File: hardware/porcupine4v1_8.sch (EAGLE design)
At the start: 32 parts, among them X1 PROGCON

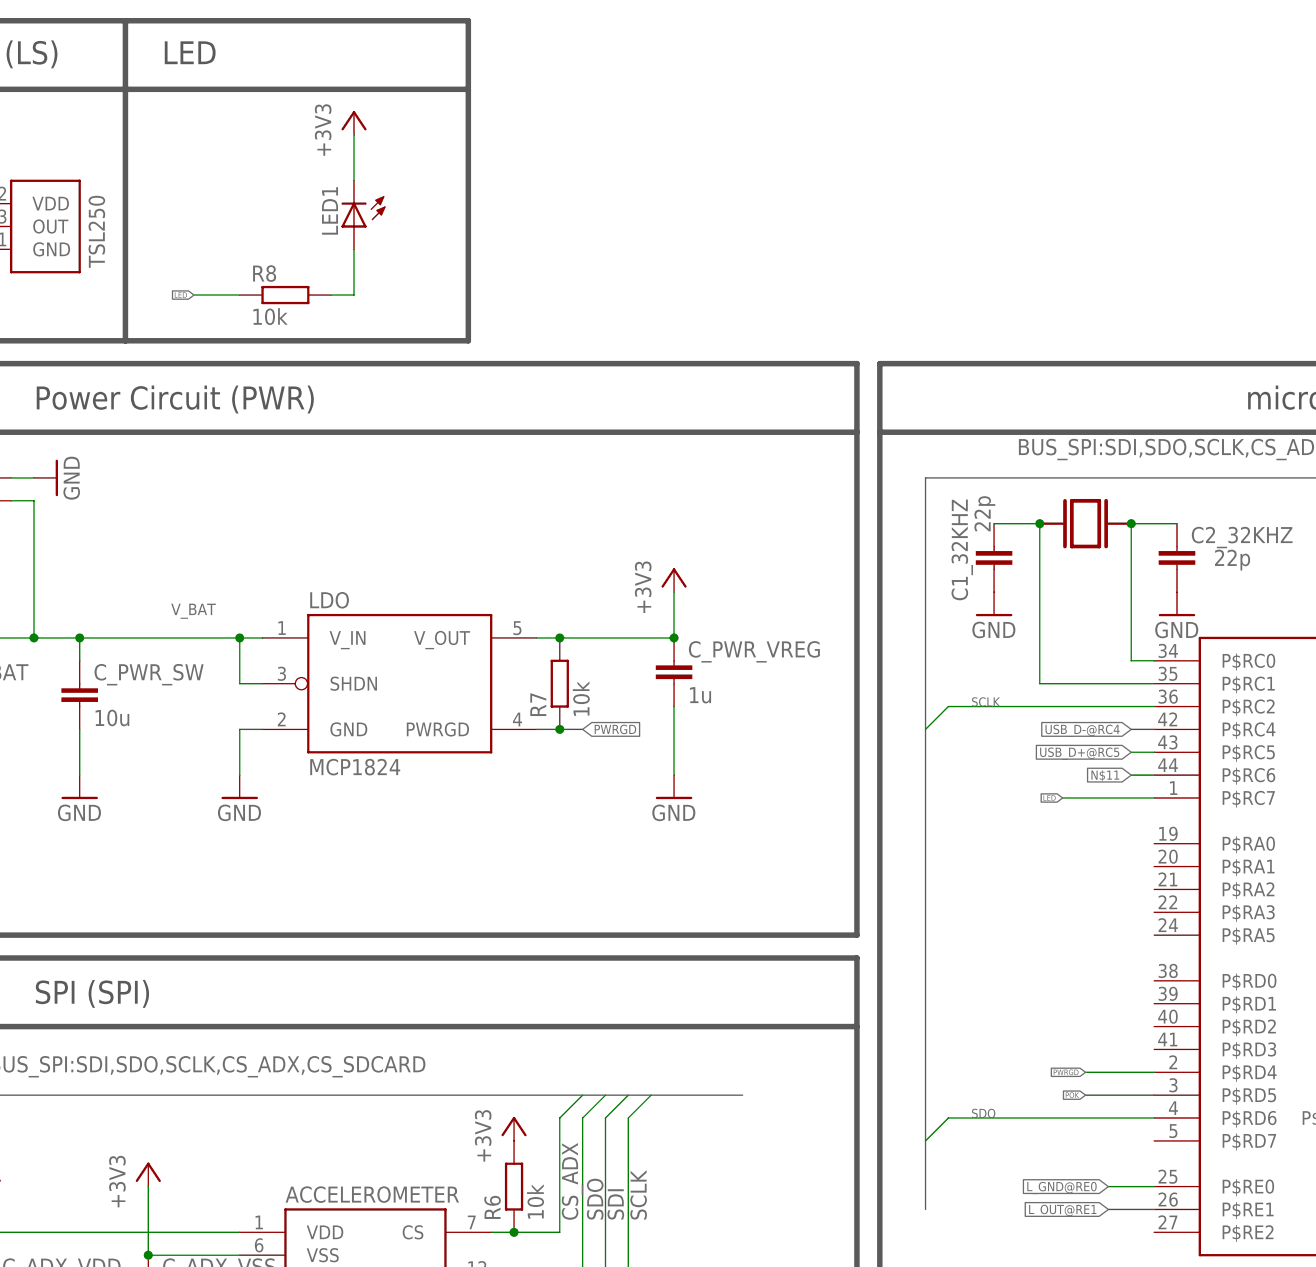
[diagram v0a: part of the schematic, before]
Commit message: porcupine4v1_8: added extension pins
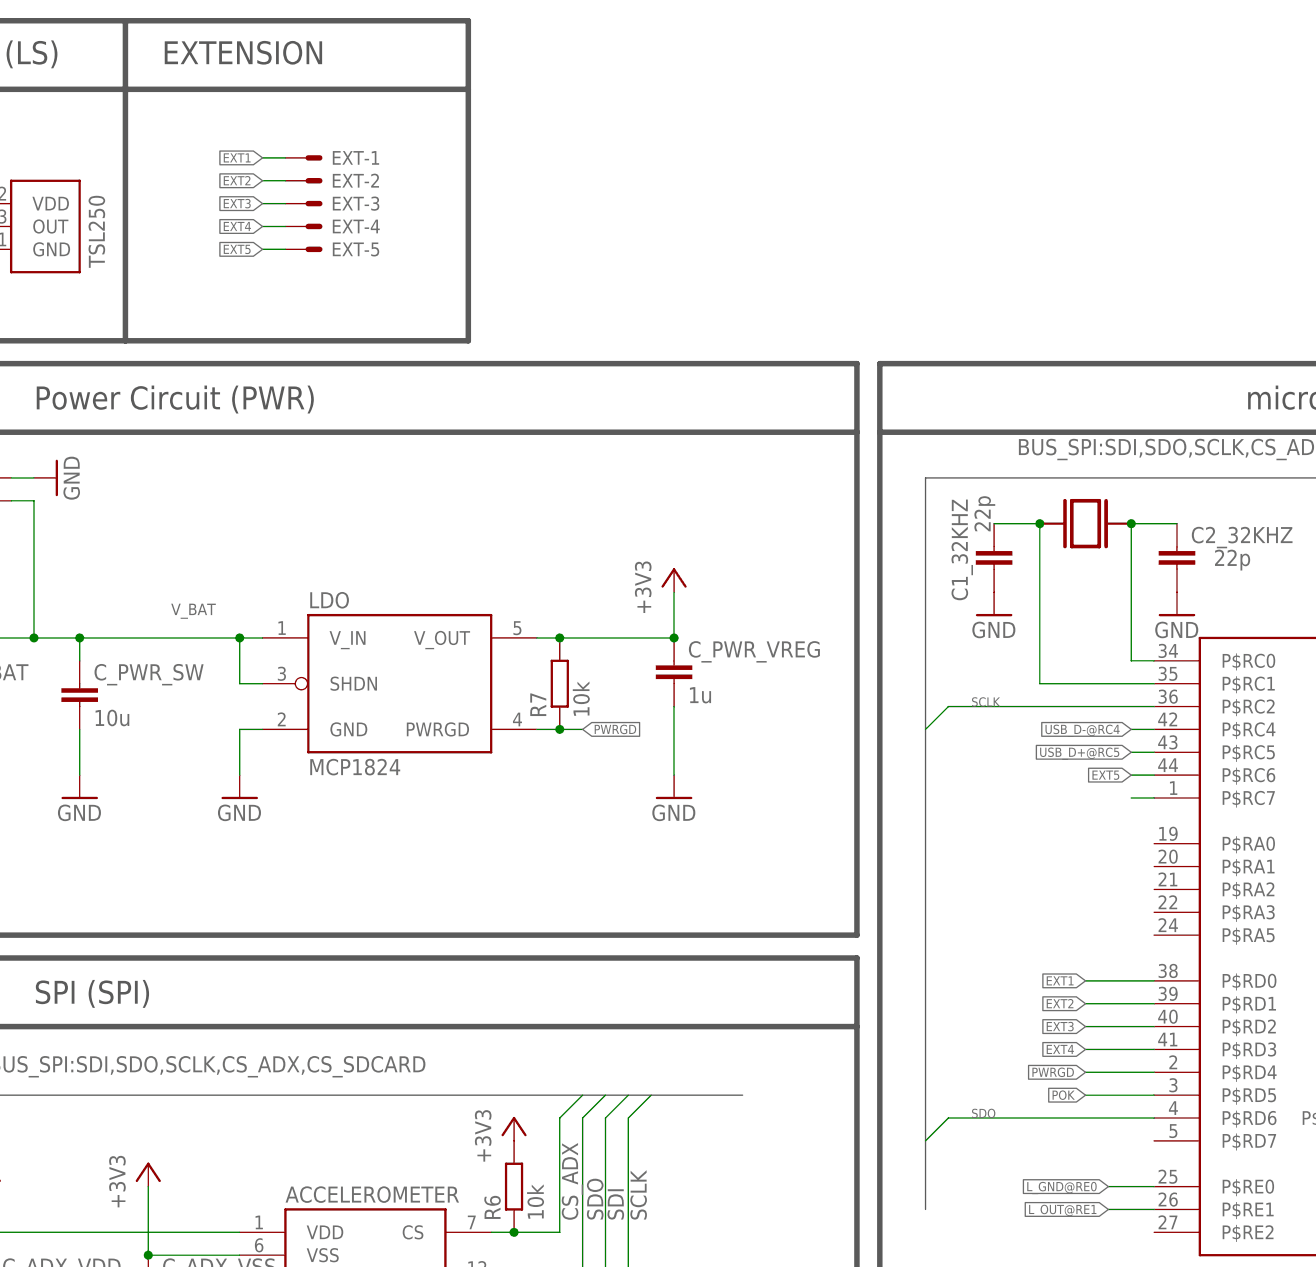
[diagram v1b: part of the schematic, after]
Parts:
- removed LED1: (no value), led:LEDCHIPLED_0805
- removed R8: 10k, rcl:R-EU_R0603
- added EXT: PROGCON, HedgehogLib:PROGCON
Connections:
- removed net LED: PIC_CONTROLLER.P$RC7, R8.1
- removed net N$11: PIC_CONTROLLER.P$RC6
- new net EXT1: EXT-1.S, PIC_CONTROLLER.P$RD0
- new net EXT2: EXT-2.S, PIC_CONTROLLER.P$RD1
- new net EXT3: EXT-3.S, PIC_CONTROLLER.P$RD2
- new net EXT4: EXT-4.S, PIC_CONTROLLER.P$RD3
- new net EXT5: EXT-5.S, PIC_CONTROLLER.P$RC6
- net +3V3: no longer LED1.C
- net N$4: now also PIC_CONTROLLER.P$RC7; no longer LED1.A, R8.2
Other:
- note added: "EXTENSION"
- note removed: "LED"
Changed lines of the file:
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@@
 <part name="LDO" library="HedgehogLib" deviceset="MCP1824" device=""/>
 <part name="BAT" library="con-molex" deviceset="53?-02" device="048"/>
-<part name="R8" library="rcl" deviceset="R-EU_" device="R0603" value="10k"/>
-<part name="+3V12" library="supply1" deviceset="+3V3" device=""/>
-<part name="LED1" library="led" deviceset="LED" device="CHIPLED_0805"/>
+<part name="EXT" library="HedgehogLib" deviceset="PROGCON" device=""/>
 </parts>
 <sheets>
@@
 <wire x1="132.08" y1="132.08" x2="132.08" y2="160.02" width="0.6096" layer="97"/>
 <wire x1="93.98" y1="132.08" x2="132.08" y2="132.08" width="0.6096" layer="97"/>
-<text x="98.044" y="162.814" size="2.54" layer="97">LED</text>
+<text x="98.044" y="162.814" size="2.54" layer="97">EXTENSION</text>
 </plain>
 <instances>
@@
 <instance part="BAT" gate="-1" x="78.74" y="114.3" rot="R180"/>
 <instance part="BAT" gate="-2" x="78.74" y="116.84" rot="R180"/>
-<instance part="R8" gate="G$1" x="111.76" y="137.16"/>
-<instance part="+3V12" gate="G$1" x="119.38" y="157.48"/>
-<instance part="LED1" gate="G$1" x="119.38" y="144.78" rot="R180"/>
+<instance part="EXT" gate="-1" x="114.3" y="152.4" smashed="yes">
+<attribute name="NAME" x="116.84" y="151.638" size="1.524" layer="95"/>
+</instance>
+<instance part="EXT" gate="-2" x="114.3" y="149.86"/>
+<instance part="EXT" gate="-3" x="114.3" y="147.32"/>
+<instance part="EXT" gate="-4" x="114.3" y="144.78"/>
+<instance part="EXT" gate="-5" x="114.3" y="142.24"/>
 </instances>
 <busses>
@@
 <pinref part="+3V17" gate="G$1" pin="+3V3"/>
 <pinref part="R3" gate="G$1" pin="2"/>
-</segment>
-<segment>
-<pinref part="+3V12" gate="G$1" pin="+3V3"/>
-<pinref part="LED1" gate="G$1" pin="C"/>
-<wire x1="119.38" y1="149.86" x2="119.38" y2="154.94" width="0.1524" layer="91"/>
 </segment>
 </net>
@@
 <pinref part="PIC_CONTROLLER" gate="G$1" pin="P$RD5"/>
 <wire x1="208.28" y1="48.26" x2="200.66" y2="48.26" width="0.1524" layer="91"/>
-<label x="200.66" y="48.26" size="0.6096" layer="95" rot="R180" xref="yes"/>
+<label x="200.66" y="48.26" size="1.016" layer="95" rot="R180" xref="yes"/>
 </segment>
 </net>
@@
 <pinref part="12MHZ_RESONATOR" gate="G$1" pin="1"/>
 <wire x1="243.84" y1="55.88" x2="259.08" y2="55.88" width="0.1524" layer="91"/>
-</segment>
-</net>
-<net name="N$11" class="0">
-<segment>
-<pinref part="PIC_CONTROLLER" gate="G$1" pin="P$RC6"/>
-<wire x1="208.28" y1="83.82" x2="205.74" y2="83.82" width="0.1524" layer="91"/>
-<label x="205.74" y="83.82" size="1.016" layer="95" rot="R180" xref="yes"/>
 </segment>
 </net>
@@
 <pinref part="PIC_CONTROLLER" gate="G$1" pin="P$RD4"/>
 <wire x1="208.28" y1="50.8" x2="200.66" y2="50.8" width="0.1524" layer="91"/>
-<label x="200.66" y="50.8" size="0.6096" layer="95" rot="R180" xref="yes"/>
-</segment>
-</net>
-<net name="LED" class="0">
+<label x="200.66" y="50.8" size="1.016" layer="95" rot="R180" xref="yes"/>
+</segment>
+</net>
+<net name="EXT1" class="0">
+<segment>
+<pinref part="EXT" gate="-1" pin="S"/>
+<wire x1="111.76" y1="152.4" x2="109.22" y2="152.4" width="0.1524" layer="91"/>
+<label x="109.22" y="152.4" size="1.016" layer="95" rot="R180" xref="yes"/>
+</segment>
+<segment>
+<pinref part="PIC_CONTROLLER" gate="G$1" pin="P$RD0"/>
+<wire x1="208.28" y1="60.96" x2="200.66" y2="60.96" width="0.1524" layer="91"/>
+<label x="200.66" y="60.96" size="1.016" layer="95" rot="R180" xref="yes"/>
+</segment>
+</net>
+<net name="EXT2" class="0">
+<segment>
+<pinref part="EXT" gate="-2" pin="S"/>
+<wire x1="111.76" y1="149.86" x2="109.22" y2="149.86" width="0.1524" layer="91"/>
+<label x="109.22" y="149.86" size="1.016" layer="95" rot="R180" xref="yes"/>
+</segment>
+<segment>
+<pinref part="PIC_CONTROLLER" gate="G$1" pin="P$RD1"/>
+<wire x1="208.28" y1="58.42" x2="200.66" y2="58.42" width="0.1524" layer="91"/>
+<label x="200.66" y="58.42" size="1.016" layer="95" rot="R180" xref="yes"/>
+</segment>
+</net>
+<net name="EXT3" class="0">
+<segment>
+<pinref part="EXT" gate="-3" pin="S"/>
+<wire x1="111.76" y1="147.32" x2="109.22" y2="147.32" width="0.1524" layer="91"/>
+<label x="109.22" y="147.32" size="1.016" layer="95" rot="R180" xref="yes"/>
+</segment>
+<segment>
+<pinref part="PIC_CONTROLLER" gate="G$1" pin="P$RD2"/>
+<wire x1="208.28" y1="55.88" x2="200.66" y2="55.88" width="0.1524" layer="91"/>
+<label x="200.66" y="55.88" size="1.016" layer="95" rot="R180" xref="yes"/>
+</segment>
+</net>
+<net name="EXT4" class="0">
+<segment>
+<pinref part="EXT" gate="-4" pin="S"/>
+<wire x1="111.76" y1="144.78" x2="109.22" y2="144.78" width="0.1524" layer="91"/>
+<label x="109.22" y="144.78" size="1.016" layer="95" rot="R180" xref="yes"/>
+</segment>
+<segment>
+<pinref part="PIC_CONTROLLER" gate="G$1" pin="P$RD3"/>
+<wire x1="208.28" y1="53.34" x2="200.66" y2="53.34" width="0.1524" layer="91"/>
+<label x="200.66" y="53.34" size="1.016" layer="95" rot="R180" xref="yes"/>
+</segment>
+</net>
+<net name="EXT5" class="0">
+<segment>
+<pinref part="EXT" gate="-5" pin="S"/>
+<wire x1="111.76" y1="142.24" x2="109.22" y2="142.24" width="0.1524" layer="91"/>
+<label x="109.22" y="142.24" size="1.016" layer="95" rot="R180" xref="yes"/>
+</segment>
+<segment>
+<pinref part="PIC_CONTROLLER" gate="G$1" pin="P$RC6"/>
+<wire x1="208.28" y1="83.82" x2="205.74" y2="83.82" width="0.1524" layer="91"/>
+<label x="205.74" y="83.82" size="1.016" layer="95" rot="R180" xref="yes"/>
+</segment>
+</net>
+<net name="N$4" class="0">
 <segment>
 <pinref part="PIC_CONTROLLER" gate="G$1" pin="P$RC7"/>
-<wire x1="208.28" y1="81.28" x2="198.12" y2="81.28" width="0.1524" layer="91"/>
-<label x="198.12" y="81.28" size="0.6096" layer="95" rot="R180" xref="yes"/>
-</segment>
-<segment>
-<pinref part="R8" gate="G$1" pin="1"/>
-<wire x1="106.68" y1="137.16" x2="101.6" y2="137.16" width="0.1524" layer="91"/>
-<label x="101.6" y="137.16" size="0.6096" layer="95" rot="R180" xref="yes"/>
-</segment>
-</net>
-<net name="N$4" class="0">
-<segment>
-<pinref part="R8" gate="G$1" pin="2"/>
-<pinref part="LED1" gate="G$1" pin="A"/>
-<wire x1="119.38" y1="142.24" x2="119.38" y2="137.16" width="0.1524" layer="91"/>
-<wire x1="119.38" y1="137.16" x2="116.84" y2="137.16" width="0.1524" layer="91"/>
-</segment>
-</net>
+<wire x1="208.28" y1="81.28" x2="205.74" y2="81.28" width="0.1524" layer="91"/>
+</segment>
+</net>

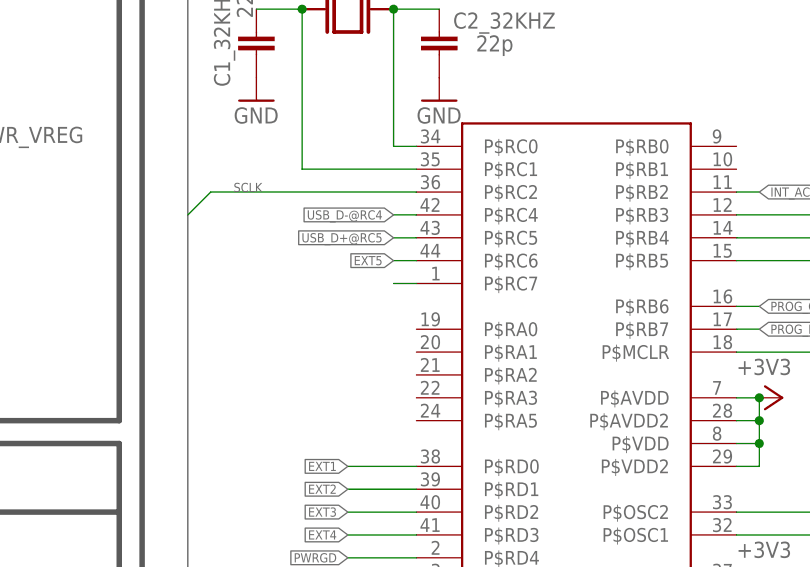
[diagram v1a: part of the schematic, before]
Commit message: porcupine4v1_8: some wires rewired
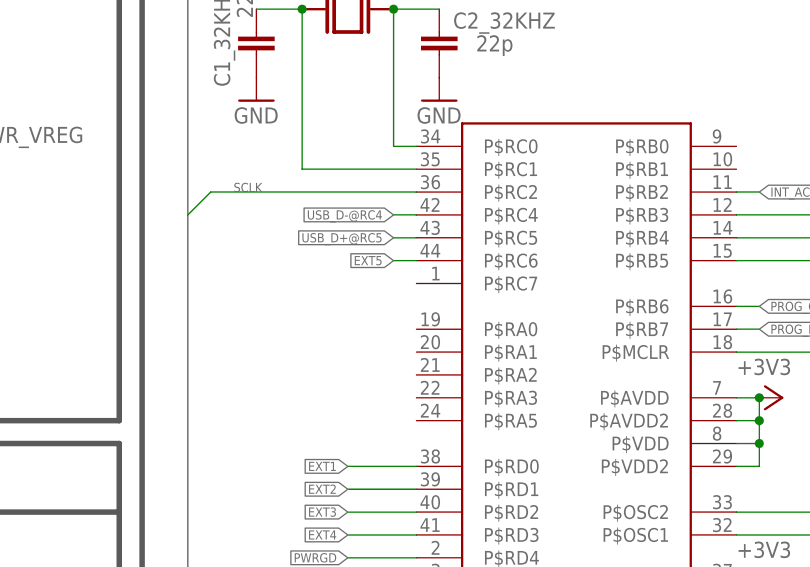
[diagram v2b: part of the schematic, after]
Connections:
- removed net N$4: PIC_CONTROLLER.P$RC7
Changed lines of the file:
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@@
-</segment>
-</net>
-<net name="N$4" class="0">
-<segment>
-<pinref part="PIC_CONTROLLER" gate="G$1" pin="P$RC7"/>
-<wire x1="208.28" y1="81.28" x2="205.74" y2="81.28" width="0.1524" layer="91"/>
 </segment>
 </net>

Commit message: 4.1.8 added bom & fixing
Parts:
- added LED1: (no value), led:LEDSML0805
- added R8: 220, rcl:R-EU_R0603
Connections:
- new net N$4: LED1.A, R8.1
- net EXT4: no longer EXT-4.S
- net EXT5: now also EXT-4.S, R8.2; no longer EXT-5.S
- net GND: now also EXT-5.S, LED1.C
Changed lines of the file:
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@@
 <part name="BAT" library="con-molex" deviceset="53?-02" device="048"/>
 <part name="EXT" library="HedgehogLib" deviceset="PROGCON" device=""/>
+<part name="R8" library="rcl" deviceset="R-EU_" device="R0603" value="220"/>
+<part name="GND2" library="supply1" deviceset="GND" device=""/>
+<part name="LED1" library="led" deviceset="LED" device="SML0805"/>
+<part name="GND10" library="supply1" deviceset="GND" device=""/>
 </parts>
 <sheets>
@@
 <wire x1="93.98" y1="132.08" x2="132.08" y2="132.08" width="0.6096" layer="97"/>
 <text x="98.044" y="162.814" size="2.54" layer="97">EXTENSION</text>
+<wire x1="132.08" y1="167.64" x2="170.18" y2="167.64" width="0.6096" layer="97"/>
+<wire x1="170.18" y1="160.02" x2="170.18" y2="167.64" width="0.6096" layer="97"/>
+<wire x1="132.08" y1="160.02" x2="170.18" y2="160.02" width="0.6096" layer="97"/>
+<wire x1="170.18" y1="132.08" x2="170.18" y2="160.02" width="0.6096" layer="97"/>
+<wire x1="132.08" y1="132.08" x2="170.18" y2="132.08" width="0.6096" layer="97"/>
+<text x="136.144" y="162.814" size="2.54" layer="97">EXTENSION</text>
 </plain>
 <instances>
@@
 <instance part="EXT" gate="-4" x="114.3" y="144.78"/>
 <instance part="EXT" gate="-5" x="114.3" y="142.24"/>
+<instance part="R8" gate="G$1" x="152.4" y="154.94" rot="R180"/>
+<instance part="GND2" gate="1" x="160.02" y="137.16"/>
+<instance part="LED1" gate="G$1" x="160.02" y="147.32"/>
+<instance part="GND10" gate="1" x="109.22" y="137.16"/>
 </instances>
 <busses>
@@
 <pinref part="GND1" gate="1" pin="GND"/>
 <wire x1="279.4" y1="48.26" x2="281.94" y2="48.26" width="0.1524" layer="91"/>
+</segment>
+<segment>
+<pinref part="LED1" gate="G$1" pin="C"/>
+<pinref part="GND2" gate="1" pin="GND"/>
+<wire x1="160.02" y1="139.7" x2="160.02" y2="142.24" width="0.1524" layer="91"/>
+</segment>
+<segment>
+<pinref part="EXT" gate="-5" pin="S"/>
+<wire x1="111.76" y1="142.24" x2="109.22" y2="142.24" width="0.1524" layer="91"/>
+<pinref part="GND10" gate="1" pin="GND"/>
+<wire x1="109.22" y1="139.7" x2="109.22" y2="142.24" width="0.1524" layer="91"/>
 </segment>
 </net>
@@
 <net name="EXT4" class="0">
 <segment>
-<pinref part="EXT" gate="-4" pin="S"/>
-<wire x1="111.76" y1="144.78" x2="109.22" y2="144.78" width="0.1524" layer="91"/>
-<label x="109.22" y="144.78" size="1.016" layer="95" rot="R180" xref="yes"/>
-</segment>
-<segment>
 <pinref part="PIC_CONTROLLER" gate="G$1" pin="P$RD3"/>
 <wire x1="208.28" y1="53.34" x2="200.66" y2="53.34" width="0.1524" layer="91"/>
@@
 <net name="EXT5" class="0">
 <segment>
-<pinref part="EXT" gate="-5" pin="S"/>
-<wire x1="111.76" y1="142.24" x2="109.22" y2="142.24" width="0.1524" layer="91"/>
-<label x="109.22" y="142.24" size="1.016" layer="95" rot="R180" xref="yes"/>
+<wire x1="111.76" y1="144.78" x2="109.22" y2="144.78" width="0.1524" layer="91"/>
+<label x="109.22" y="144.78" size="1.016" layer="95" rot="R180" xref="yes"/>
+<pinref part="EXT" gate="-4" pin="S"/>
 </segment>
 <segment>
@@
 <label x="205.74" y="83.82" size="1.016" layer="95" rot="R180" xref="yes"/>
 </segment>
-</net>
+<segment>
+<wire x1="147.32" y1="154.94" x2="139.7" y2="154.94" width="0.1524" layer="91"/>
+<label x="139.7" y="154.94" size="1.016" layer="95" rot="R180" xref="yes"/>
+<pinref part="R8" gate="G$1" pin="2"/>
+</segment>
+</net>
+<net name="N$4" class="0">
+<segment>
+<pinref part="LED1" gate="G$1" pin="A"/>
+<pinref part="R8" gate="G$1" pin="1"/>
+<wire x1="157.48" y1="154.94" x2="160.02" y2="154.94" width="0.1524" layer="91"/>
+<wire x1="160.02" y1="154.94" x2="160.02" y2="149.86" width="0.1524" layer="91"/>
+</segment>
+</net>
